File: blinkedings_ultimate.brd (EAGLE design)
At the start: 62.5 x 15.7 mm, 34 parts, among them IC1 FT232RL, T1 BC807-16, T4 BC847, T5 BC847, T6 BC847

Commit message: BC807-16 -> BC807-40
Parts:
- R14: value 5.6k -> 12k
- T1: value BC807-16 -> BC807-40
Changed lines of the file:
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@@
 <element name="C4" library="resistor" package="C0603" value="100nF" x="22.733" y="70.4596" rot="R90"/>
 <element name="U$3" library="avr-6" package="SO20L$" value="TINY2313-*S*" x="32.258" y="72.39"/>
-<element name="T1" library="transistor" package="SOT23-BEC" value="BC807-16" x="47.0916" y="77.724" rot="R270"/>
+<element name="T1" library="transistor" package="SOT23-BEC" value="BC807-40" x="47.0916" y="77.724" rot="R270"/>
 <element name="R7" library="resistor" package="R0603" value="22k" x="41.783" y="67.2592" rot="R90"/>
 <element name="R8" library="resistor" package="R0603" value="27k" x="41.8084" y="74.0156" rot="R90"/>
@@
 <element name="R12" library="resistor" package="R0603" value="10k" x="44.0436" y="70.5866" rot="R90"/>
 <element name="R13" library="resistor" package="R0603" value="10k" x="44.0436" y="77.724" rot="R90"/>
-<element name="R14" library="resistor" package="R0603" value="5.6k" x="41.7322" y="77.724" rot="R270"/>
+<element name="R14" library="resistor" package="R0603" value="12k" x="41.7322" y="77.724" rot="R270"/>
 </elements>
 <signals>

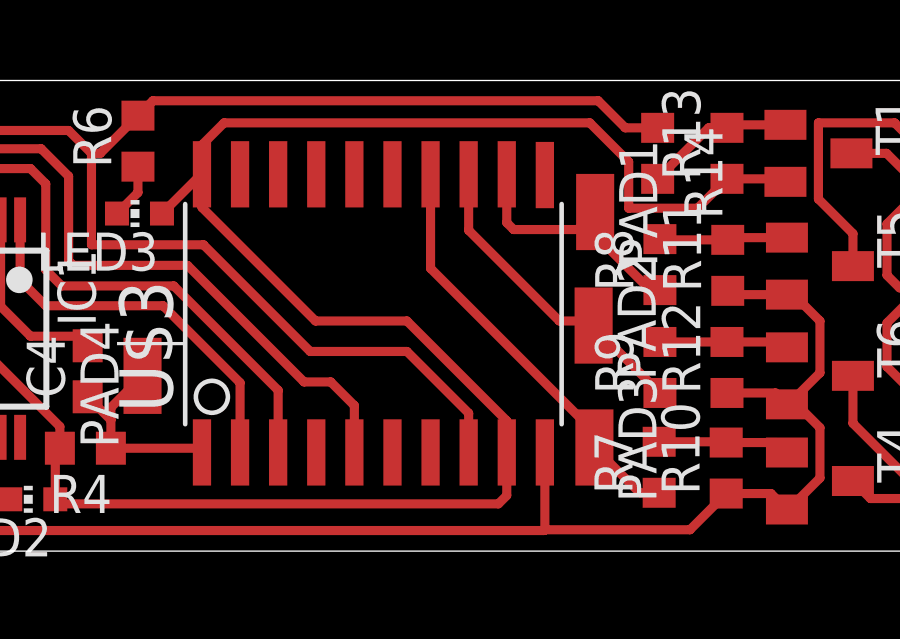
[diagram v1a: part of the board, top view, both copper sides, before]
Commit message: fix wrong sck/miso/mosi pins
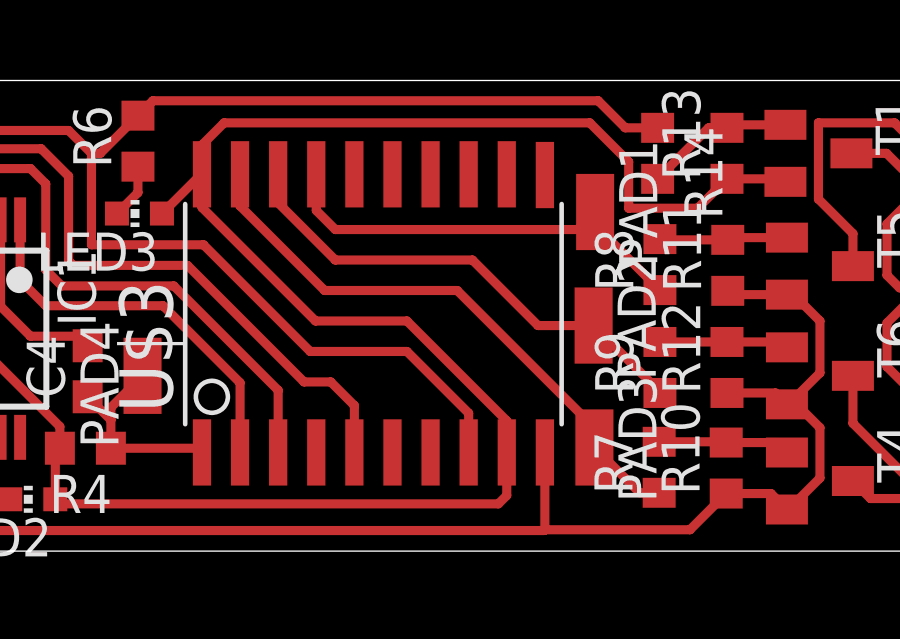
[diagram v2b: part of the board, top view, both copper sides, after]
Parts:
- PAD1: value SCK -> MOSI
- PAD3: value MOSI -> SCK
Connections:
- removed net N$14: PAD2.1, R9.1, U$3.13
- new net N$22: PAD1.1, R8.1, U$3.17
- net N$15: now also PAD2.1, R9.1, U$3.18; no longer PAD1.1, R8.1, U$3.12
- net N$16: now also U$3.19; no longer U$3.14
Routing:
- net N$22: track 0.00 -> 14.5 mm
- net N$14: track 10.7 -> 0.00 mm
- net N$15: track 8.36 -> 16.3 mm
- net N$16: track 14.2 -> 19.4 mm
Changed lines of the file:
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@@
 </class>
 </classes>
-<designrules name="smd *">
+<designrules name="smd">
 <description language="de">&lt;b&gt;EAGLE Design Rules&lt;/b&gt;
 &lt;p&gt;
@@
 <element name="C3" library="resistor" package="SMC_C" value="4.7uF" x="7.7216" y="72.2884" rot="R90"/>
 <element name="U$2" library="usb" package="USB-A-SMD" value="USB-PLUG-A-SMD" x="-6.35" y="72.39"/>
-<element name="PAD1" library="wirepad" package="SMD1,27-2,54" value="SCK" x="39.6494" y="75.7682" rot="R180"/>
+<element name="PAD1" library="wirepad" package="SMD1,27-2,54" value="MOSI" x="39.6494" y="75.7682" rot="R180"/>
 <element name="PAD2" library="wirepad" package="SMD1,27-2,54" value="MISO" x="39.5986" y="71.9836" rot="R180"/>
-<element name="PAD3" library="wirepad" package="SMD1,27-2,54" value="MOSI" x="39.624" y="67.9196" rot="R180"/>
+<element name="PAD3" library="wirepad" package="SMD1,27-2,54" value="SCK" x="39.624" y="67.9196" rot="R180"/>
 <element name="PAD4" library="wirepad" package="SMD1,27-2,54" value="RESET" x="24.5618" y="70.3072"/>
 <element name="R4" library="resistor" package="R0603" value="10k" x="22.6568" y="67.8942" rot="R180"/>
@@
 <wire x1="20.481" y1="73.499" x2="20.481" y2="75.507" width="0.3048" layer="1"/>
 </signal>
-<signal name="N$14">
-<contactref element="U$3" pad="13"/>
-<wire x1="35.433" y1="77.0255" x2="35.433" y2="75.1586" width="0.3048" layer="1"/>
-<contactref element="PAD2" pad="1"/>
-<wire x1="35.433" y1="75.1586" x2="38.4556" y2="72.136" width="0.3048" layer="1"/>
-<wire x1="38.4556" y1="72.136" x2="39.4462" y2="72.136" width="0.3048" layer="1"/>
-<wire x1="39.4462" y1="72.136" x2="39.5986" y2="71.9836" width="0.3048" layer="1"/>
-<contactref element="R9" pad="1"/>
-<wire x1="39.5986" y1="71.9836" x2="39.5986" y2="71.5654" width="0.3048" layer="1"/>
-<wire x1="39.5986" y1="71.5654" x2="39.9796" y2="71.5654" width="0.3048" layer="1"/>
-<wire x1="39.9796" y1="71.5654" x2="41.8084" y2="69.7366" width="0.3048" layer="1"/>
-</signal>
-<signal name="N$15">
-<contactref element="U$3" pad="12"/>
-<contactref element="PAD1" pad="1"/>
-<contactref element="R8" pad="1"/>
-<wire x1="36.703" y1="77.0255" x2="36.703" y2="75.4126" width="0.3048" layer="1"/>
-<wire x1="36.703" y1="75.4126" x2="36.9316" y2="75.184" width="0.3048" layer="1"/>
-<wire x1="36.9316" y1="75.184" x2="39.0652" y2="75.184" width="0.3048" layer="1"/>
-<wire x1="39.0652" y1="75.184" x2="39.2684" y2="75.3872" width="0.3048" layer="1"/>
-<wire x1="39.2684" y1="75.3872" x2="39.6494" y2="75.7682" width="0.3048" layer="1"/>
-<wire x1="41.8084" y1="73.1656" x2="41.49" y2="73.1656" width="0.3048" layer="1"/>
-<wire x1="41.49" y1="73.1656" x2="39.2684" y2="75.3872" width="0.3048" layer="1"/>
-</signal>
 <signal name="N$16">
-<contactref element="U$3" pad="14"/>
+<contactref element="R7" pad="1"/>
+<contactref element="U$3" pad="19"/>
 <contactref element="PAD3" pad="1"/>
-<contactref element="R7" pad="1"/>
-<wire x1="34.163" y1="77.0255" x2="34.163" y2="73.8886" width="0.3048" layer="1"/>
-<wire x1="34.163" y1="73.8886" x2="39.624" y2="68.4276" width="0.3048" layer="1"/>
-<wire x1="39.624" y1="68.4276" x2="39.624" y2="67.9196" width="0.3048" layer="1"/>
-<wire x1="39.624" y1="67.9196" x2="41.1344" y2="66.4092" width="0.3048" layer="1"/>
-<wire x1="41.1344" y1="66.4092" x2="41.783" y2="66.4092" width="0.3048" layer="1"/>
+<wire x1="41.783" y1="66.4092" x2="41.1344" y2="66.4092" width="0.3048" layer="1"/>
+<wire x1="41.1344" y1="66.4092" x2="39.624" y2="67.9196" width="0.3048" layer="1"/>
+<wire x1="39.624" y1="67.9196" x2="39.624" y2="68.58" width="0.3048" layer="1"/>
+<wire x1="39.624" y1="68.58" x2="35.052" y2="73.152" width="0.3048" layer="1"/>
+<wire x1="35.052" y1="73.152" x2="30.6324" y2="73.152" width="0.3048" layer="1"/>
+<wire x1="30.6324" y1="73.152" x2="27.813" y2="75.9714" width="0.3048" layer="1"/>
+<wire x1="27.813" y1="75.9714" x2="27.813" y2="77.0255" width="0.3048" layer="1"/>
 </signal>
 <signal name="CLK">
@@
 <wire x1="43.4322" y1="78.574" x2="41.7322" y2="76.874" width="0.3048" layer="1"/>
 </signal>
+<signal name="N$22">
+<contactref element="R8" pad="1"/>
+<contactref element="U$3" pad="17"/>
+<contactref element="PAD1" pad="1"/>
+<wire x1="41.8084" y1="73.1656" x2="39.6494" y2="75.3246" width="0.3048" layer="1"/>
+<wire x1="39.6494" y1="75.3246" x2="39.6494" y2="75.7682" width="0.3048" layer="1"/>
+<wire x1="39.6494" y1="75.7682" x2="39.0652" y2="75.184" width="0.3048" layer="1"/>
+<wire x1="39.0652" y1="75.184" x2="30.988" y2="75.184" width="0.3048" layer="1"/>
+<wire x1="30.988" y1="75.184" x2="30.353" y2="75.819" width="0.3048" layer="1"/>
+<wire x1="30.353" y1="75.819" x2="30.353" y2="77.0255" width="0.3048" layer="1"/>
+</signal>
+<signal name="N$15">
+<contactref element="R9" pad="1"/>
+<contactref element="U$3" pad="18"/>
+<contactref element="PAD2" pad="1"/>
+<wire x1="41.8084" y1="69.7366" x2="41.8084" y2="69.7738" width="0.3048" layer="1"/>
+<wire x1="41.8084" y1="69.7738" x2="39.5986" y2="71.9836" width="0.3048" layer="1"/>
+<wire x1="39.5986" y1="71.9836" x2="37.7444" y2="71.9836" width="0.3048" layer="1"/>
+<wire x1="37.7444" y1="71.9836" x2="35.56" y2="74.168" width="0.3048" layer="1"/>
+<wire x1="35.56" y1="74.168" x2="30.988" y2="74.168" width="0.3048" layer="1"/>
+<wire x1="30.988" y1="74.168" x2="29.083" y2="76.073" width="0.3048" layer="1"/>
+<wire x1="29.083" y1="76.073" x2="29.083" y2="77.0255" width="0.3048" layer="1"/>
+</signal>
 </signals>
